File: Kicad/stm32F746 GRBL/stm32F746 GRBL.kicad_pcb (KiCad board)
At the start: 2 copper layers, 130 x 80 mm, 146 parts, among them CN1 PinHeader_1x08_P2.54mm_Vertic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, CN2 PinHeader_1x06_P2.54mm_Vertic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, CN3 PinHeader_1x10_P2.54mm_Vertic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, CN4 PinHeader_1x08_P2.54mm_Vertic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, J1 X-Axis, J10 Conn_01x04, J11 Conn_01x04, J12 Conn_01x04, J13 Power Input, J14 Input 1-8, J15 Input 9-16, J16 Output, J17 PWM-1, J18 PWM-2, J19 PWM-3, J2 Y-Axis, J20 PWM-4, J21 4-20MA or 0-10V, J3 Z-Axis, J4 A-Axis, J5 B-Axis, J6 C-Axis, J7 Conn_01x04, J8 Conn_01x04, J9 Conn_01x04, Q1 BSS138, Q2 BSS138, Q3 BSS138, Q4 BSS138, Q5 MMBT5087, Q6 BSP170, U1 MCP23008-xSS, U10 LMR51430, U11 LM1117MP-3.3, U12 ULN2803A, U13 XTR111AxDGQ, U14 TSV911RILT, U2 MCP23008-xSS, U3 24LC64, U4 MCP23017_SS, U5 TLP521-4, U6 TLP521-4, U7 TLP521-4, U8 TLP521-4, U9 74AHCT1G125

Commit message: wip kicad
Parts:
- C9, U11: moved to F.Cu
- moved R24 74.5 mm to (149.2, 117.1)
- moved U14 70.3 mm to (146.2, 116.9), turned to 90 degrees
- moved C13 68.7 mm to (150.0, 120.2)
- moved C12 68.7 mm to (146.2, 120.2), turned to 180 degrees
- moved D8 45.6 mm to (140.2, 120.4)
- moved R30 40.2 mm to (141.4, 123.5)
- moved R29 38.4 mm to (122.5, 117.7), turned to 180 degrees
- moved F1 33.3 mm to (159.4, 123.2)
- moved Q6 32.2 mm to (123.8, 123.9), turned to -90 degrees
- moved C11 29.2 mm to (134.7, 120.4), turned to 180 degrees
- moved C9 23.6 mm to (147.1, 133.3), turned to 180 degrees
- moved C14 21.9 mm to (136.2, 130.4), turned to 90 degrees
- moved U11 21.4 mm to (148.0, 126.7)
- moved R28 16.8 mm to (130.0, 125.7)
- moved R25 16.5 mm to (133.2, 131.4)
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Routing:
- net Vdrive: track 0.00 -> 321.6 mm
- net GND: track 0.00 -> 296.4 mm, vias 0 -> 42
- net +3.3VP: track 0.00 -> 182.0 mm, vias 0 -> 3
- net /Driver/ENABLE: track 42.0 -> 178.0 mm, vias 0 -> 1
- net PWM3: track 0.00 -> 111.2 mm, vias 0 -> 5
- net PWM4: track 0.00 -> 110.4 mm, vias 0 -> 3
- net /Driver/X-STEP: track 0.00 -> 83.6 mm, vias 0 -> 1
- net /Driver/A-STEP: track 0.00 -> 80.9 mm, vias 0 -> 1
- net /Driver/X-DIR: track 0.00 -> 78.1 mm, vias 0 -> 1
- net /Driver/A-DIR: track 0.00 -> 75.9 mm, vias 0 -> 1
- net I2C_SCL: track 0.00 -> 73.6 mm, vias 0 -> 3
- net I2C_SDA: track 0.00 -> 71.9 mm, vias 0 -> 4
- net PWM2: track 0.00 -> 66.5 mm, vias 0 -> 4
- net PWM1: track 0.00 -> 62.4 mm, vias 0 -> 2
- net INPUT_INT_1: track 0.00 -> 54.6 mm, vias 0 -> 1
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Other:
- board text added: "4-20"
- board text added: "mA"

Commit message: wip Kicad
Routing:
- net GND: track 296.4 -> 704.6 mm, vias 42 -> 55
- net RESET: track 0.00 -> 134.4 mm, vias 0 -> 7
- net Net-(A5-CFG4): track 0.00 -> 23.9 mm
- net Net-(A5-CFG3): track 0.00 -> 21.6 mm
- net CPU_Z-STEP: track 2.17 -> 18.5 mm, vias 0 -> 1
- net Net-(A3-CFG4): track 0.00 -> 11.6 mm
- net Net-(A2-CFG4): track 0.00 -> 11.6 mm
- net Net-(A6-CFG4): track 0.00 -> 11.6 mm
- net CPU_Z-DIR: track 2.17 -> 13.6 mm, vias 0 -> 1
- net Net-(A3-CFG3): track 0.00 -> 10.8 mm
- net Net-(A2-CFG3): track 0.00 -> 10.8 mm
- net Net-(A6-CFG3): track 0.00 -> 10.8 mm
- net Net-(A5-CFG2): track 0.00 -> 10.7 mm
- net Net-(A3-CFG2): track 0.00 -> 10.7 mm
- net Net-(A2-CFG2): track 0.00 -> 10.7 mm
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
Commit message: wip Kicad
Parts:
- moved RN4 0.98 mm to (88.2, 104.3)
- moved RN3 0.33 mm to (88.2, 79.8)
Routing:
- net +5VP: track 42.6 -> 171.9 mm, vias 2 -> 6
- net /Driver/ENABLE: track 178.0 -> 218.3 mm, vias 1 -> 2
- net GND: track 704.6 -> 729.5 mm, vias 55 -> 56
- net Vdrive: track 321.8 -> 329.2 mm, vias 0 -> 6
- net Net-(J13-Pin_1): track 0.00 -> 5.08 mm
- net /Input/INPUT_1: track 4.40 -> 8.07 mm
- net /Input/INPUT_2: track 6.84 -> 10.5 mm
- net /Input/INPUT_3: track 9.24 -> 12.9 mm
- net /Input/INPUT_4: track 12.0 -> 15.7 mm
- net Net-(RN3D-R4.1): track 0.00 -> 3.54 mm
- net Net-(RN3C-R3.1): track 0.00 -> 3.54 mm
- net Net-(RN3B-R2.1): track 0.00 -> 3.54 mm
- net Net-(RN3A-R1.1): track 0.00 -> 3.54 mm
- net Net-(RN4D-R4.1): track 0.00 -> 3.45 mm
- net Net-(RN4B-R2.1): track 0.00 -> 3.45 mm
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
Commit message: wip Kicad.
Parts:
- added G***: LOGO, LOGO, F.Cu at (176.2, 114.0)
- moved C13 15.3 mm to (134.8, 122.0), turned to -90 degrees
- moved R29 13.6 mm to (118.2, 130.6), turned to -90 degrees
- moved C3 13.0 mm to (143.3, 113.6)
- moved U3 13.0 mm to (147.3, 113.5)
- moved C10 12.7 mm to (127.4, 113.1)
- moved C11 12.7 mm to (127.3, 110.1)
- moved D8 12.7 mm to (132.8, 110.1)
- moved U13 12.7 mm to (128.8, 116.2)
- moved R24 12.0 mm to (137.9, 121.2), turned to 180 degrees
- moved Q5 11.8 mm to (122.9, 113.0)
- moved R28 11.8 mm to (122.9, 116.3)
- moved R25 11.8 mm to (127.1, 121.3)
- moved R26 11.8 mm to (127.1, 119.4)
- moved C14 11.8 mm to (130.1, 120.3)
- moved C12 11.6 mm to (134.8, 118.2), turned to 90 degrees
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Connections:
- net SPINDLESPEED renamed PWM_4-20MA
- RJ4 pad 2: Net-(A1-CFG4) -> Net-(A1-CFG3)
- RJ5 pad 2: Net-(A1-CFG3) -> Net-(A1-CFG4)
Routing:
- net GND: track 729.5 -> 1042.9 mm, vias 56 -> 75
- net +3.3V: track 4.45 -> 62.9 mm, vias 0 -> 2
- net PWM_4-20MA: track 0.00 -> 29.8 mm, vias 0 -> 2
- net Net-(D8-K): track 0.00 -> 29.5 mm
- net /Output/ERROR_FLAG: track 0.00 -> 22.2 mm, vias 0 -> 2
- net /Output/4_20MA_OR_0_10V_DISABLE: track 0.00 -> 20.8 mm, vias 0 -> 2
- net Net-(Q5-B): track 0.00 -> 13.4 mm
- net Net-(Q5-C): track 0.00 -> 12.6 mm
- net I2C_SDA: track 71.3 -> 83.5 mm
- net Net-(U13-VIN): track 0.00 -> 11.7 mm, vias 0 -> 2
- net I2C_SCL: track 73.5 -> 85.2 mm
- net Net-(A1-CFG4): track 0.00 -> 11.6 mm
- net Net-(A5-CFG4): track 23.9 -> 12.3 mm
- net Net-(A1-CFG3): track 0.00 -> 10.9 mm
- net Net-(A5-CFG3): track 21.6 -> 10.8 mm
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
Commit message: wip kicad
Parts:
- F1: value Polyfuse -> Fuse; footprint Fuse:Fuse_1812_4532Metric_Pad1.30x3.40mm_HandSolder -> Fuse:Fuseholder_Littelfuse_Nano2_154x
- moved U11 11.7 mm to (154.8, 115.3)
- moved C9 11.6 mm to (154.2, 122.2)
- moved F1 7.23 mm to (157.7, 130.2), turned to 180 degrees
- moved C7 2.24 mm to (172.8, 121.6)
- moved C8 2.06 mm to (172.8, 119.4)
- moved R13 1.73 mm to (164.4, 88.1)
- moved U9 1.47 mm to (164.7, 85.4)
- moved D7 1.42 mm to (161.2, 85.4)
- moved R29 1.21 mm to (119.2, 130.0), turned to 0 degrees
- moved J21 0.41 mm to (111.6, 129.5)
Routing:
- net +3.3VP: track 189.8 -> 284.7 mm, vias 5 -> 11
- net Vdrive: track 338.3 -> 396.5 mm, vias 6 -> 7
- net GND: track 1042.9 -> 1099.7 mm, vias 75 -> 81
- net Net-(J13-Pin_1): track 5.08 -> 29.6 mm, vias 0 -> 2
- net +5VP: track 171.9 -> 195.4 mm, vias 6 -> 7
- net Net-(U10-SW): track 0.00 -> 9.40 mm
- net Net-(D9-A2): track 14.4 -> 18.6 mm
- net Net-(U10-FB): track 0.00 -> 4.03 mm
- net /Driver/ENABLE: track 218.5 -> 221.9 mm
- net CPU_ENABLE: track 41.2 -> 39.4 mm
- net Net-(U10-CB): track 0.00 -> 1.70 mm
- net PWM_4-20MA: track 29.8 -> 29.0 mm
- net /Driver/B-DIR: track 42.7 -> 43.4 mm
- added copper zone on B.Cu, net GND

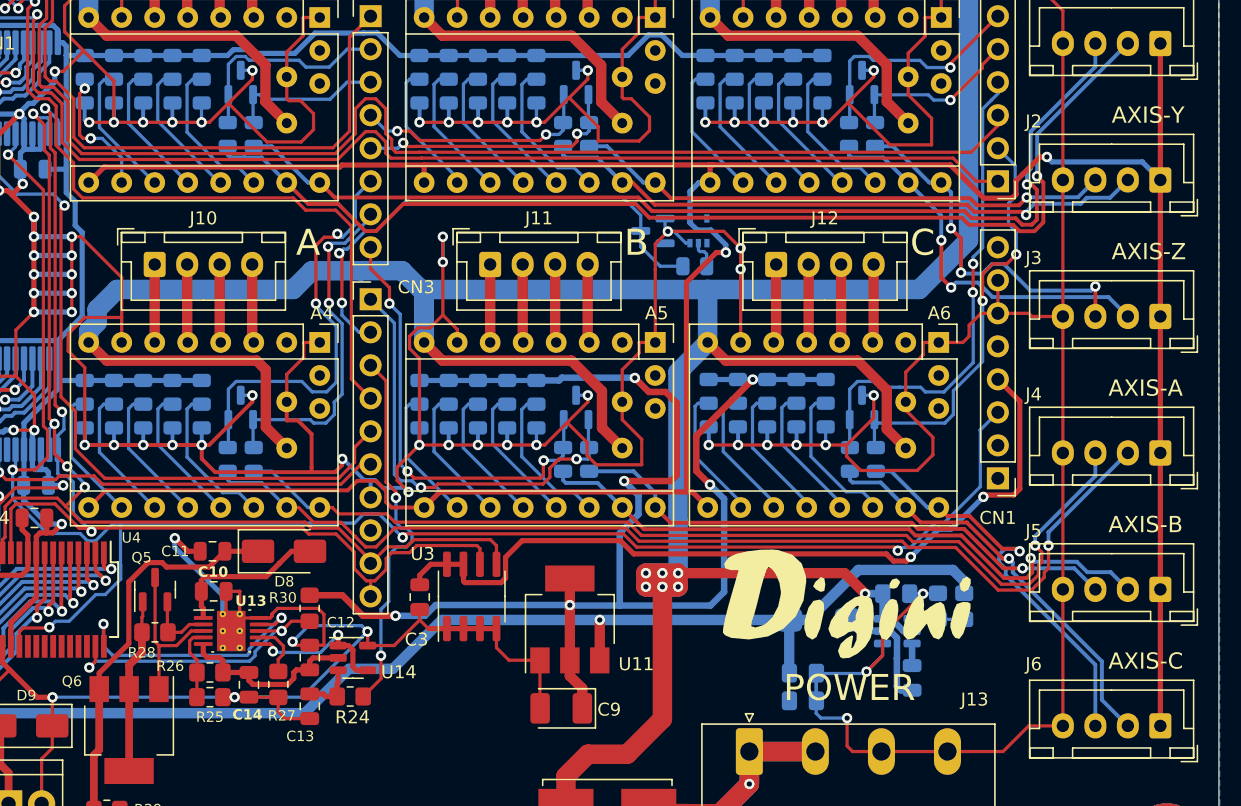
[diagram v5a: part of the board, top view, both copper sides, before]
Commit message: Adding MCP230xx driver and config
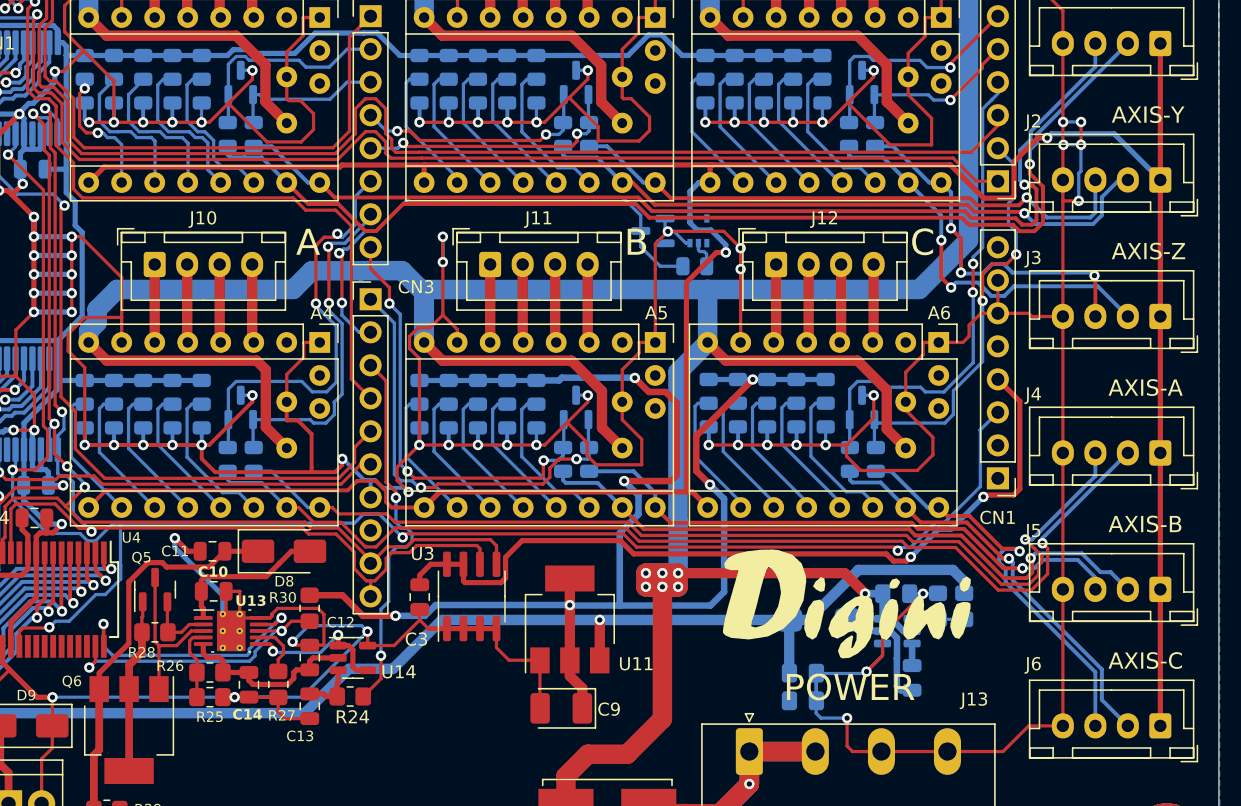
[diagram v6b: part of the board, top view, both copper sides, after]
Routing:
- net GND: track 1099.7 -> 1109.8 mm, vias 81 -> 86
- net /Driver/Y-DIR: track 41.6 -> 44.4 mm
- net /Driver/ENABLE: track 221.9 -> 224.3 mm
- net /Driver/Y-STEP: track 47.3 -> 48.5 mm
- net Net-(A1-CFG2): track 10.8 -> 12.0 mm
- net Net-(A1-CFG3): track 10.9 -> 12.1 mm
- net Net-(A1-CFG1): track 10.7 -> 11.8 mm
- net /Driver/B-DIR: track 43.4 -> 44.4 mm
- net /Driver/A-DIR: track 75.9 -> 76.8 mm
- net /Driver/Z-STEP: track 30.4 -> 31.0 mm
- net /Driver/X-DIR: track 79.2 -> 79.7 mm
